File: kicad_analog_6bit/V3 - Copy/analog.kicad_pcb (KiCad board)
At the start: 2 copper layers, 53.9 x 23.2 mm, 37 parts, among them P1 Conn_02x06_Odd_Even, P2 Conn_01x04, P3 Conn_01x06, P4 Conn_01x03_ODD, P5 Conn_01x03_EVEN, P6 Conn_01x01, P7 Conn_01x01, U1 MAX9108, U2 MAX9108, U3 TS12A44514DR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

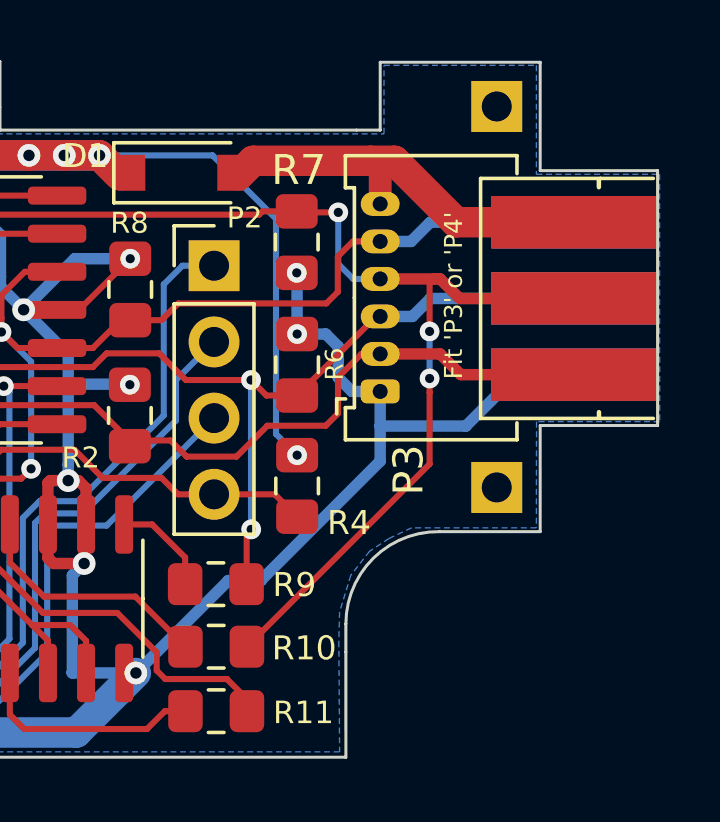
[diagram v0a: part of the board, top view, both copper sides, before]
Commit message: Extend P4 pads on analog board
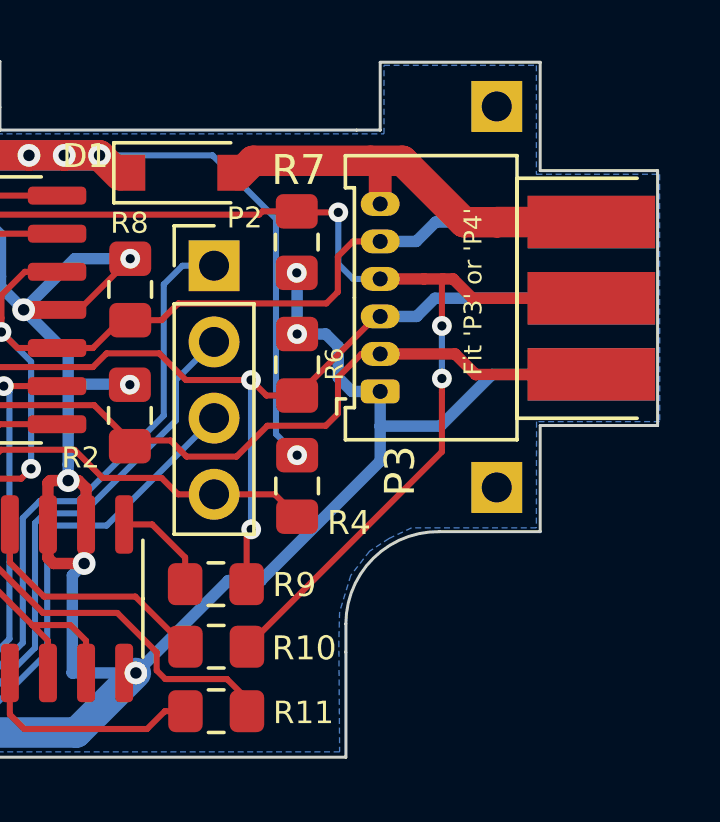
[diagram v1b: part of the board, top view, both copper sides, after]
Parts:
- P3: footprint Connector_Molex:Molex_PicoBlade_53048-0610_1x06_P1.25mm_Horizontal_Custom2 -> Connector_Molex:Molex_PicoBlade_53048-0610_1x06_P1.25mm_Horizontal
- moved P4 1.22 mm to (84.7, 39.2)
- moved P5 1.22 mm to (84.7, 39.2)
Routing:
- net /AGREEN: track 60.4 -> 61.1 mm
- net /VCC_IN: track 13.9 -> 14.5 mm
- net /GND: track 205.8 -> 206.4 mm
- net /ARED: track 82.6 -> 83.2 mm
- net /ASYNC: track 33.9 -> 34.5 mm
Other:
- board text added: "Pin 1"
- board text removed: "Pin1"
